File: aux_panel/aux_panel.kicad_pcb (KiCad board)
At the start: 2 copper layers, 20.3 x 133.4 mm, 5 parts

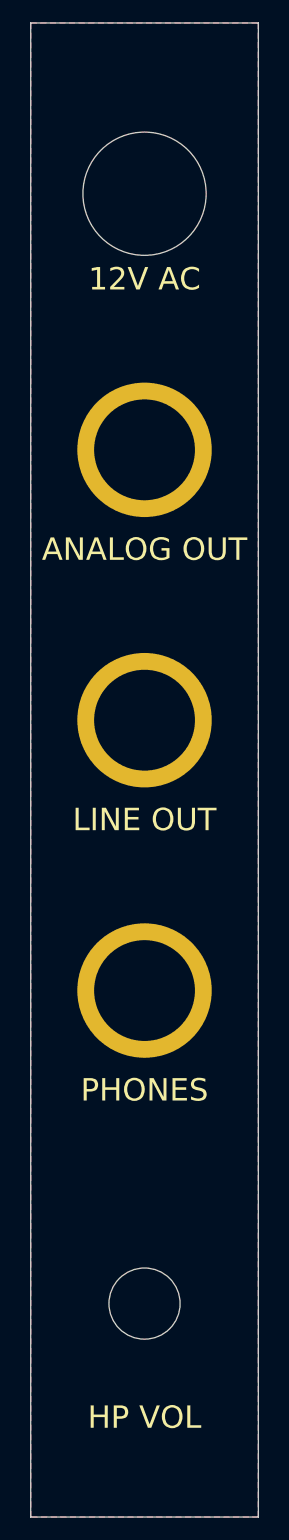
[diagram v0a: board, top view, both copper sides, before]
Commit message: Complete aux panel PCB
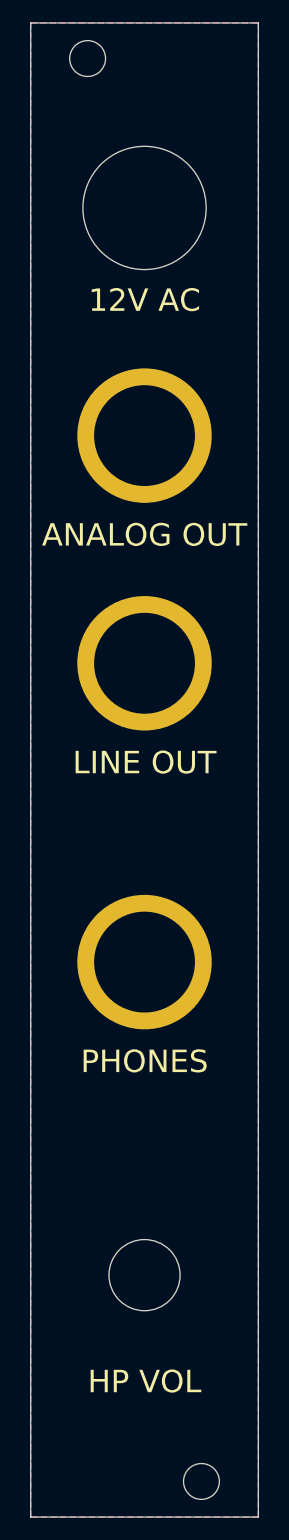
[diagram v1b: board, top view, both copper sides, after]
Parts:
- added H6: Mounting Hole, MountingHole:MountingHole_3.2mm_M3, F.Cu at (106.7, 47.6)
- added H7: Mounting Hole, MountingHole:MountingHole_3.2mm_M3, F.Cu at (116.8, 174.6)
- moved H5 5.08 mm to (111.8, 101.6)
- moved H1 2.54 mm to (111.8, 156.2)
- moved H2 2.54 mm to (111.8, 128.3)
- moved H3 1.27 mm to (111.8, 61.0)
- moved H4 1.27 mm to (111.8, 81.3)
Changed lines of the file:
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@@
   (title_block
     (title "Minidrone Aux Panel")
-    (date "2022-05-30")
+    (date "2022-06-04")
     (rev "0.1")
     (company "Max Proskauer")
@@
   (setup
     (pad_to_mask_clearance 0)
-    (grid_origin 111.76 50.8)
+    (grid_origin 111.76 111.125)
     (pcbplotparams
       (layerselection 0x00010fc_ffffffff)
@@
       (outputformat 1)
       (mirror false)
-      (drillshape 1)
+      (drillshape 0)
       (scaleselection 1)
-      (outputdirectory "")
+      (outputdirectory "gerber")
     )
   )
   (net 0 "")
   (footprint "kosmo-lib:Hole_Jack" (layer "F.Cu")
-    (at 111.76 82.55)
+    (at 111.76 81.28)
     (property "Sheetfile" "aux_panel.kicad_sch")
     (property "Sheetname" "")
@@
     (pad "1" thru_hole circle (at 0 0) (size 12 12) (drill 9) (layers *.Cu *.Mask))
   )
+  (footprint "MountingHole:MountingHole_3.2mm_M3" (layer "F.Cu")
+    (at 116.84 174.625)
+    (descr "Mounting Hole 3.2mm, no annular, M3")
+    (tags "mounting hole 3.2mm no annular m3")
+    (property "Sheetfile" "aux_panel.kicad_sch")
+    (property "Sheetname" "")
+    (attr exclude_from_pos_files)
+    (fp_text reference "H7" (at 0 -4.2) (layer "F.SilkS") hide
+      (effects (font (size 1 1) (thickness 0.15)))
+    )
+    (fp_text value "Mounting Hole" (at 0 4.2) (layer "F.Fab") hide
+      (effects (font (size 1 1) (thickness 0.15)))
+    )
+    (fp_text user "${REFERENCE}" (at 0 0) (layer "F.Fab") hide
+      (effects (font (size 1 1) (thickness 0.15)))
+    )
+    (fp_circle (center 0 0) (end 3.2 0) (layer "Cmts.User") (width 0.15) (fill none))
+    (fp_circle (center 0 0) (end 3.45 0) (layer "F.CrtYd") (width 0.05) (fill none))
+    (pad "" np_thru_hole circle (at 0 0) (size 3.2 3.2) (drill 3.2) (layers *.Cu *.Mask))
+  )
   (footprint "kosmo-lib:Hole_Barrel_Jack" (layer "F.Cu")
-    (at 111.76 59.69)
+    (at 111.76 60.96)
     (property "Sheetfile" "aux_panel.kicad_sch")
     (property "Sheetname" "")
@@
     (pad "" np_thru_hole circle (at 0 0) (size 11 11) (drill 11) (layers F&B.Cu *.Mask))
   )
+  (footprint "MountingHole:MountingHole_3.2mm_M3" (layer "F.Cu")
+    (at 106.68 47.625)
+    (descr "Mounting Hole 3.2mm, no annular, M3")
+    (tags "mounting hole 3.2mm no annular m3")
+    (property "Sheetfile" "aux_panel.kicad_sch")
+    (property "Sheetname" "")
+    (attr exclude_from_pos_files)
+    (fp_text reference "H6" (at 0 -4.2) (layer "F.SilkS") hide
+      (effects (font (size 1 1) (thickness 0.15)))
+    )
+    (fp_text value "Mounting Hole" (at 0 4.2) (layer "F.Fab") hide
+      (effects (font (size 1 1) (thickness 0.15)))
+    )
+    (fp_text user "${REFERENCE}" (at 0 0) (layer "F.Fab") hide
+      (effects (font (size 1 1) (thickness 0.15)))
+    )
+    (fp_circle (center 0 0) (end 3.2 0) (layer "Cmts.User") (width 0.15) (fill none))
+    (fp_circle (center 0 0) (end 3.45 0) (layer "F.CrtYd") (width 0.05) (fill none))
+    (pad "" np_thru_hole circle (at 0 0) (size 3.2 3.2) (drill 3.2) (layers *.Cu *.Mask))
+  )
   (footprint "kosmo-lib:Hole_Jack" (layer "F.Cu")
-    (at 111.76 130.81)
+    (at 111.76 128.27)
     (property "Sheetfile" "aux_panel.kicad_sch")
     (property "Sheetname" "")
@@
   )
   (footprint "kosmo-lib:Module_Headphone_Amp" (layer "F.Cu")
-    (at 111.76 158.75 180)
+    (at 111.76 156.21 180)
     (property "Sheetfile" "aux_panel.kicad_sch")
     (property "Sheetname" "")
@@
   )
   (footprint "kosmo-lib:Hole_Jack" (layer "F.Cu")
-    (at 111.76 106.68)
+    (at 111.76 101.6)
     (property "Sheetfile" "aux_panel.kicad_sch")
     (property "Sheetname" "")
@@
     (pad "1" thru_hole circle (at 0 0) (size 12 12) (drill 9) (layers *.Cu *.Mask))
   )
-  (gr_line (start 101.6 139.7) (end 121.92 139.7) (layer "Cmts.User") (width 0.15))
-  (gr_line (start 101.6 63.5) (end 121.92 63.5) (layer "Cmts.User") (width 0.15))
+  (gr_line (start 101.6 60.96) (end 121.92 60.96) (layer "Cmts.User") (width 0.15))
   (gr_line (start 101.6 101.6) (end 121.92 101.6) (layer "Cmts.User") (width 0.15))
-  (gr_line (start 101.6 82.55) (end 121.92 82.55) (layer "Cmts.User") (width 0.15))
-  (gr_circle (center 111.76 158.75) (end 119.38 158.75) (layer "Cmts.User") (width 0.1) (fill none))
-  (gr_line (start 101.6 158.75) (end 121.92 158.75) (layer "Cmts.User") (width 0.15))
-  (gr_line (start 101.6 120.65) (end 121.92 120.65) (layer "Cmts.User") (width 0.15))
+  (gr_line (start 101.6 81.28) (end 121.92 81.28) (layer "Cmts.User") (width 0.15))
+  (gr_circle (center 111.76 156.21) (end 119.38 156.21) (layer "Cmts.User") (width 0.1) (fill none))
+  (gr_line (start 101.6 156.21) (end 121.92 156.21) (layer "Cmts.User") (width 0.15))
+  (gr_line (start 101.6 128.27) (end 121.92 128.27) (layer "Cmts.User") (width 0.15))
   (gr_rect (start 101.6 44.45) (end 121.92 177.8) (layer "Edge.Cuts") (width 0.1) (fill none))
   (gr_line (start 111.76 44.45) (end 111.76 177.8) (layer "F.Fab") (width 0.1))
@@
     (effects (font (size 1 1) (thickness 0.15)) (justify mirror))
   )
-  (gr_text "12V AC" (at 111.76 67.31) (layer "F.SilkS")
+  (gr_text "12V AC" (at 111.76 69.215) (layer "F.SilkS")
     (effects (font (size 2 2) (thickness 0.3)))
   )
-  (gr_text "HP VOL" (at 111.76 168.91) (layer "F.SilkS")
+  (gr_text "HP VOL" (at 111.76 165.735) (layer "F.SilkS")
     (effects (font (size 2 2) (thickness 0.3)))
   )
-  (gr_text "PHONES" (at 111.76 139.7) (layer "F.SilkS")
+  (gr_text "PHONES" (at 111.76 137.16) (layer "F.SilkS")
     (effects (font (size 2 2) (thickness 0.3)))
   )
